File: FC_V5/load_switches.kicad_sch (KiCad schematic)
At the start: 20 parts

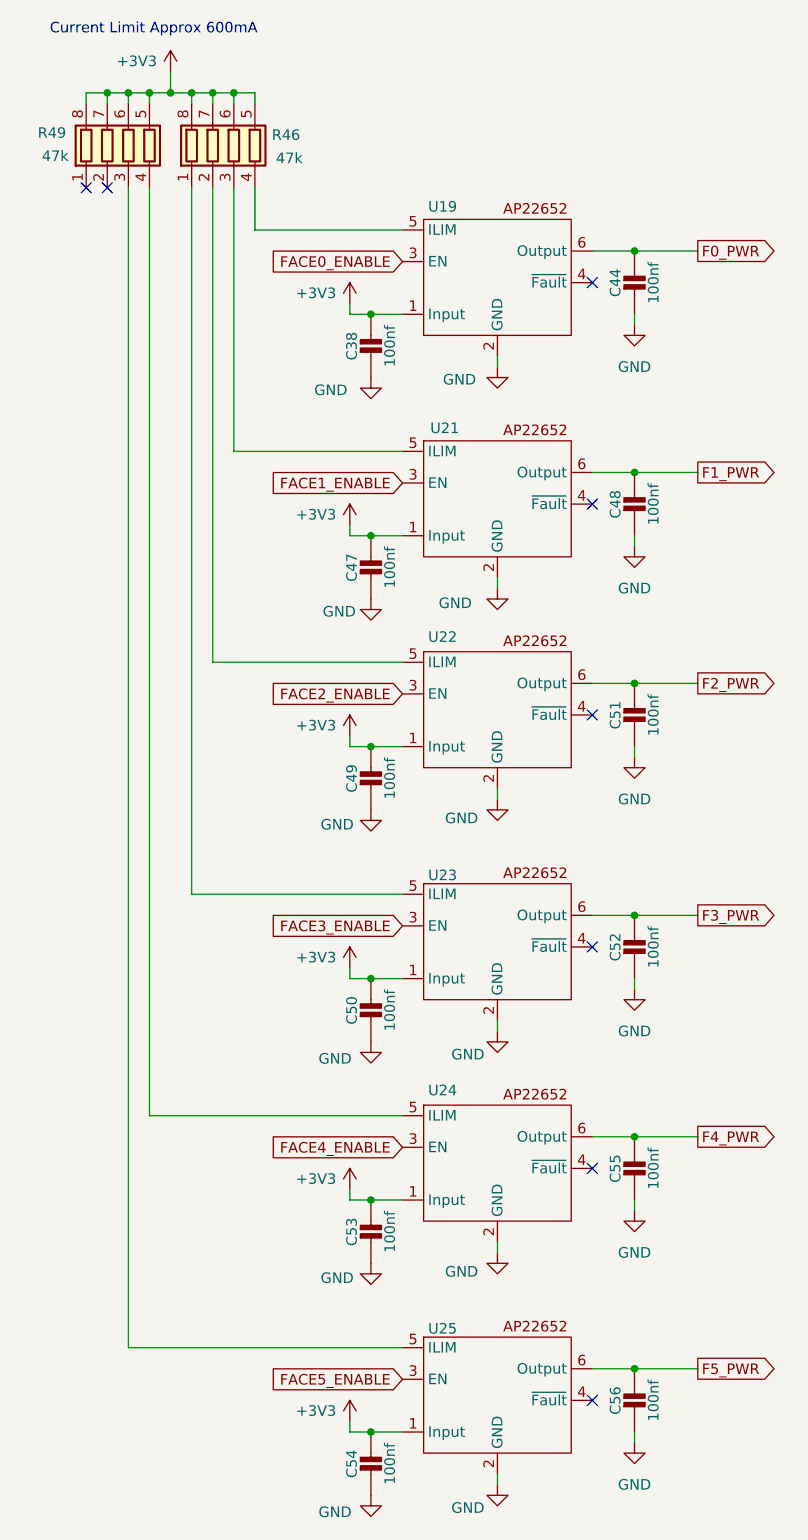
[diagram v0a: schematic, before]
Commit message: Wired Up Load Switches
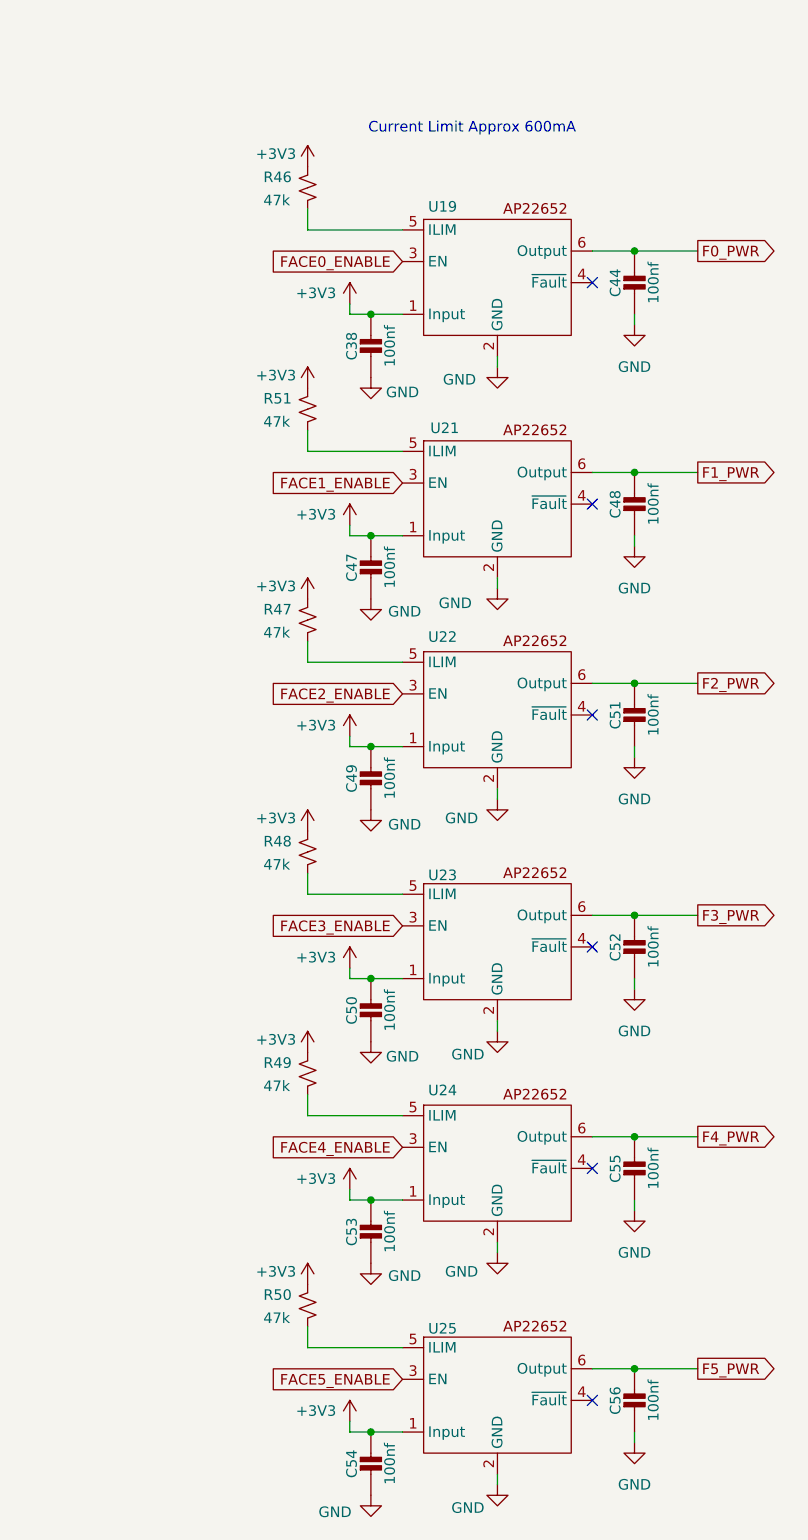
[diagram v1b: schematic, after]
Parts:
- removed R46, R49: 47k, Resistor_SMD:R_Array_Convex_4x0402, symbol Device:R_Pack04
- added R46, R47, R48, R49, R50, R51: 47k, Resistor_SMD:R_0603_1608Metric, symbol Device:R_Small_US
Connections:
- net +3V3: now also R46.1, R47.1, R48.1, R49.1, R50.1, R51.1
- net at U23.5 (ILIM): now also R48.2
- net at U22.5 (ILIM): now also R47.2
- net at U21.5 (ILIM): now also R51.2
- net at U19.5 (ILIM): now also R46.2
- net at U25.5 (ILIM): now also R50.2
- net at U24.5 (ILIM): now also R49.2
- no-connect marks 8 -> 6

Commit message: More Layout!
Molex Connectors and Load Switches are in place
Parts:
- U19, U21, U22, U23, U24, U25: value ~ -> AP22652
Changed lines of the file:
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@@
 	(text "Current Limit Approx 600mA"
 		(exclude_from_sim no)
-		(at 71.882 27.178 0)
+		(at 74.422 26.162 0)
 		(effects
 			(font
@@
 			)
 		)
-		(property "Value" "~"
+		(property "Value" "AP22652"
 			(at 74.93 168.91 0)
 			(effects
@@
 			)
 		)
-		(property "Value" "~"
+		(property "Value" "AP22652"
 			(at 74.93 86.36 0)
 			(effects
@@
 			)
 		)
-		(property "Value" "~"
+		(property "Value" "AP22652"
 			(at 74.93 114.3 0)
 			(effects
@@
 			)
 		)
-		(property "Value" "~"
+		(property "Value" "AP22652"
 			(at 74.93 140.97 0)
 			(effects
@@
 			)
 		)
-		(property "Value" "~"
+		(property "Value" "AP22652"
 			(at 74.93 60.96 0)
 			(effects
@@
 			)
 		)
-		(property "Value" "~"
+		(property "Value" "AP22652"
 			(at 74.93 34.29 0)
 			(effects

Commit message: Refreshed TCA Layout
Using the automotive grade part now!
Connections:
- net F3_PWR: now also C55.1, U24.6 (Output); no longer C52.1, U23.6 (Output)
- net F4_PWR: now also C52.1, U23.6 (Output); no longer C55.1, U24.6 (Output)
- net FACE3_ENABLE: now also U24.3 (EN); no longer U23.3 (EN)
- net FACE4_ENABLE: now also U23.3 (EN); no longer U24.3 (EN)
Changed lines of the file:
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@@
+		)
+	)
+	(global_label "F3_PWR"
+		(shape output)
+		(at 99.06 148.59 0)
+		(fields_autoplaced yes)
+		(effects
+			(font
+				(size 1.27 1.27)
+			)
+			(justify left)
+		)
+		(property "Intersheetrefs" "${INTERSHEET_REFS}"
+			(at 109.3023 148.59 0)
+			(effects
+				(font
+					(size 1.27 1.27)
+				)
+				(justify left)
+				(hide yes)
+			)
 		)
 	)
@@
 		)
 	)
-	(global_label "F4_PWR"
-		(shape output)
-		(at 99.06 148.59 0)
-		(fields_autoplaced yes)
-		(effects
-			(font
-				(size 1.27 1.27)
-			)
-			(justify left)
-		)
-		(property "Intersheetrefs" "${INTERSHEET_REFS}"
-			(at 109.3023 148.59 0)
-			(effects
-				(font
-					(size 1.27 1.27)
-				)
-				(justify left)
-				(hide yes)
-			)
-		)
-	)
-	(global_label "FACE4_ENABLE"
-		(shape input)
-		(at 63.5 149.86 180)
-		(fields_autoplaced yes)
-		(effects
-			(font
-				(size 1.27 1.27)
-			)
-			(justify right)
-		)
-		(property "Intersheetrefs" "${INTERSHEET_REFS}"
-			(at 46.7263 149.86 0)
-			(effects
-				(font
-					(size 1.27 1.27)
-				)
-				(justify right)
-				(hide yes)
-			)
-		)
-	)
 	(global_label "F5_PWR"
 		(shape output)
@@
 				)
 				(justify left)
+				(hide yes)
+			)
+		)
+	)
+	(global_label "FACE4_ENABLE"
+		(shape input)
+		(at 63.5 123.19 180)
+		(fields_autoplaced yes)
+		(effects
+			(font
+				(size 1.27 1.27)
+			)
+			(justify right)
+		)
+		(property "Intersheetrefs" "${INTERSHEET_REFS}"
+			(at 46.7263 123.19 0)
+			(effects
+				(font
+					(size 1.27 1.27)
+				)
+				(justify right)
 				(hide yes)
 			)
@@
 		)
 	)
-	(global_label "F3_PWR"
-		(shape output)
-		(at 99.06 121.92 0)
+	(global_label "FACE3_ENABLE"
+		(shape input)
+		(at 63.5 149.86 180)
 		(fields_autoplaced yes)
 		(effects
@@
 				(size 1.27 1.27)
 			)
-			(justify left)
+			(justify right)
 		)
 		(property "Intersheetrefs" "${INTERSHEET_REFS}"
-			(at 109.3023 121.92 0)
+			(at 46.7263 149.86 0)
 			(effects
 				(font
 					(size 1.27 1.27)
 				)
-				(justify left)
+				(justify right)
 				(hide yes)
 			)
@@
 		)
 	)
-	(global_label "FACE3_ENABLE"
-		(shape input)
-		(at 63.5 123.19 180)
+	(global_label "F4_PWR"
+		(shape output)
+		(at 99.06 121.92 0)
 		(fields_autoplaced yes)
 		(effects
@@
 				(size 1.27 1.27)
 			)
-			(justify right)
+			(justify left)
 		)
 		(property "Intersheetrefs" "${INTERSHEET_REFS}"
-			(at 46.7263 123.19 0)
+			(at 109.3023 121.92 0)
 			(effects
 				(font
 					(size 1.27 1.27)
 				)
-				(justify right)
+				(justify left)
 				(hide yes)
 			)

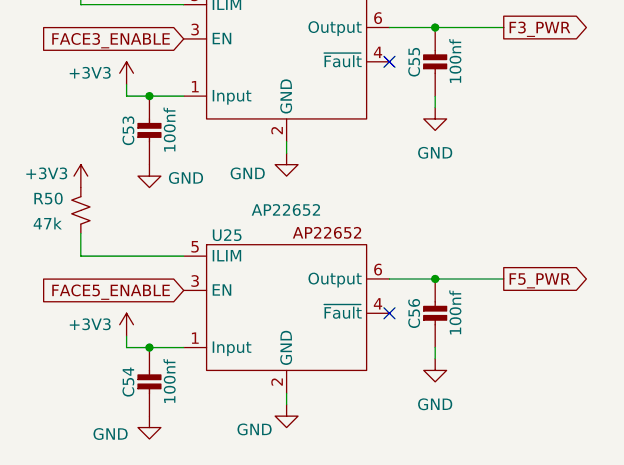
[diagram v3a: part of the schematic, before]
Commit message: Almost Done with Layout!
Just been the VReg reset circuit and the V_RF Regulator and we are ready to rock and roll
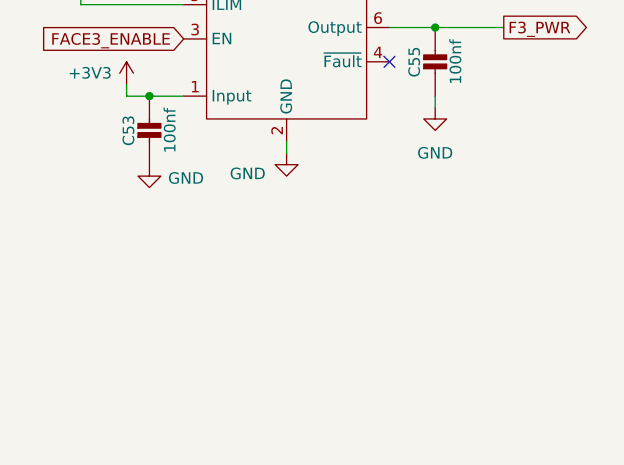
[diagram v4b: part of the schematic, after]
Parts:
- removed C54, C56: 100nf, Capacitor_SMD:C_0402_1005Metric, symbol Adafruit ItsyBitsy RP2040-eagle-import:CAP_CERAMIC_0402NO
- removed R50: 47k, Resistor_SMD:R_0603_1608Metric, symbol Device:R_Small_US
- removed U25: AP22652, SOT26:SOT26, symbol Power_Management:AP22652
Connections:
- no-connect marks 6 -> 5
